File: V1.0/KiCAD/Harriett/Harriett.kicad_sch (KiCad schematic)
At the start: 21 parts, among them J1 Conn_02x08_Odd_Even, Q1 TP0604, Q2 2N3904, U1 ButtonPad_2x2, U2 DFRobotMP3PlayerMini, U4 BlackPill_F401CC

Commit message: Catchup
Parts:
- removed C1: 470u 16V, symbol Device:C_Polarized_Small
- removed J1: Conn_02x08_Odd_Even, symbol Connector_Generic:Conn_02x08_Odd_Even
- removed U1: ButtonPad_2x2, symbol UKMaker:ButtonPad_2x2
- added BT4: AA, symbol Device:Battery_Cell
- added D1: D, symbol Device:D
- added Q3: NPN, symbol Simulation_SPICE:NPN
- added Q4: Q_PMOS_DGS, symbol Device:Q_PMOS_DGS
- added R3: 22R, symbol Device:R
- added R4: R, symbol Device:R
- added R8: 100K, symbol Device:R
- added S1, S2, S3, S4: ~, SparkFun-KSA_SEALED_TAC_SWITCH, symbol Sparkfun:TAC_SWITCHKSA_SEALED
- Q1: symbol Device:Q_PMOS_DGS -> Device:Q_PMOS_SGD
- R5: value 1K -> 47k
- R6: value 1K -> 100K
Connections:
- net B10 is gone; now on net DF3_EN: U4.21 (B10)
- net +5V: now also Q1.1 (S), D1.1 (K); no longer BT3.1 (+), Q1.3 (S), R1.1
- net DF3_EN: no longer U4.19 (B1)
- net GND: now also R5.2, Q3.3 (E), R8.1, S1.2, S2.2, S3.2, S4.2
- net HARRIETT: now also U4.43 (B7), S2.4; no longer U4.39 (B3)
- net SNOOZE: now also U4.46 (B9), S4.4; no longer U4.41 (B5)
- net STOP: now also U4.45 (B8), S3.4; no longer U4.40 (B4)
- net WORK: now also U4.42 (B6), S1.4; no longer U4.20 (B2)
- net at C2.1, U2.1 (VCC): now also Q1.3 (D); no longer Q1.1 (D)
- net at U2.6 (SPK_1): now also R3.1; no longer LS1.2
- net at R5.1: now also R6.2, Q3.2 (B); no longer U4.25 (B12)
- net at U4.26 (B13): no longer R6.1
- net at U4.27 (B14): no longer R7.1
- net RST: now reaches R7.2
- net RST: now also R6.1
- net A11: no longer names the net of U4.32 (A11)
- net A12: no longer names the net of U4.33 (A12)
- net A15: no longer names the net of U4.38 (A15)
- net A6: no longer names the net of U4.16 (A6)
- net A8: no longer names the net of U4.29 (A8)
- net B15: no longer names the net of U4.28 (B15)
- net C13: no longer names the net of U4.2 (C13)
- net C14: no longer names the net of U4.3 (C14)
- net C15: no longer names the net of U4.4 (C15)
- net RX: no longer names the net of U4.31 (A10)
- net RX: no longer U2.3 (TX)
- net TX: no longer names the net of U4.30 (A9)
- net TX: no longer U2.2 (RX)
- new net: BT3.1 (+), BT4.2 (-)
- new net: Q3.1 (C), Q4.2 (G), R4.2
- new net: LS1.2, R3.2
- new net +6V: BT4.1 (+), D1.2 (A), R1.1
- new net DF3_RX: U2.3 (TX), U4.19 (B1)
- new net DF3_TX: U2.2 (RX), U4.20 (B2)
- new net EN: R7.1, R8.2
- new net VC: Q4.3 (S), R4.1
- new net VCC: Q4.1 (D)
- no-connect marks 13 -> 14
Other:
- note added: "0.6uA in shutdown mode for the power amp IC"
- note added: "5V -> 3.3V regulator on-board BlackPill is XC6219 (Marked LB2K) 25uA power consumption Specified for 2.0V to 6.0V input, absolute max 7.0V Dropout voltage 200mV So ideal for use with e.g. 3 or 4 x AA batteries"
- note added: "IRST = 3V3 / 101K + (3V3 - 0V7) / 100K = 33uA + 26uA = 59uA"
- note added: "Power consumption update max 40mW => 12mA Standby 0.017mW => 5.2uA"
- note removed: "1.5mA LED current Pins can do 8mA or 20mA with level loss"
- note removed: "5V -> 3.3V regulator on-board BlackPill is XC6219 (Marked LB2K) 25uA power consumption Specified for 2.0V to 6.0V input, absolute max 7.0V Dropout voltage 200mV So ideal for use with e.g. 3 x AA batteries"
- note removed: "Board outlines for diodes are populated with shorts"
- moved on the sheet: R1, R2

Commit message: Various updates backported from EDAWin - may be broken
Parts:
- added J1: Conn_01x04, symbol Connector_Generic:Conn_01x04
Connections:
- net +3.3V: now also J1.3 (Pin_3)
- net DF3_RX: now also U4.13 (A3); no longer U4.19 (B1)
- net DF3_TX: now also U4.12 (A2); no longer U4.20 (B2)
- net GND: now also J1.4 (Pin_4)
- net at U3.2 (RST): now also U4.19 (B1); no longer U4.12 (A2)
- net at U3.3 (DC): now also U4.20 (B2); no longer U4.13 (A3)
- net TX: now reaches U4.30 (A9)
- net TX: now also J1.2 (Pin_2)
- net RX: now reaches U4.31 (A10)
- net RX: now also J1.1 (Pin_1)
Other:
- note added: "Serial debugging"

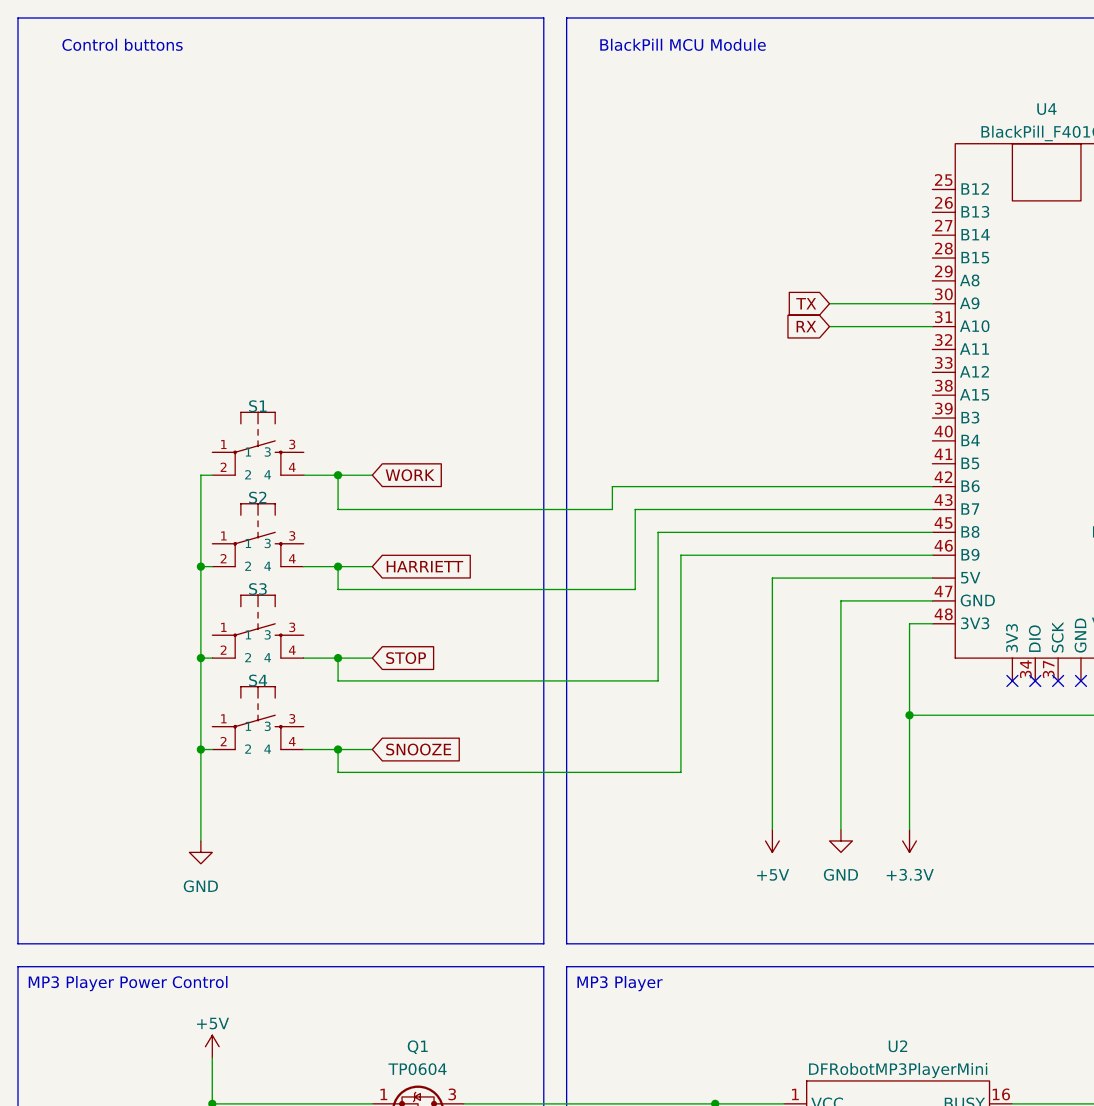
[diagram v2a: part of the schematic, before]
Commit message: Removed old Cura files. Updated schematic for PWM option
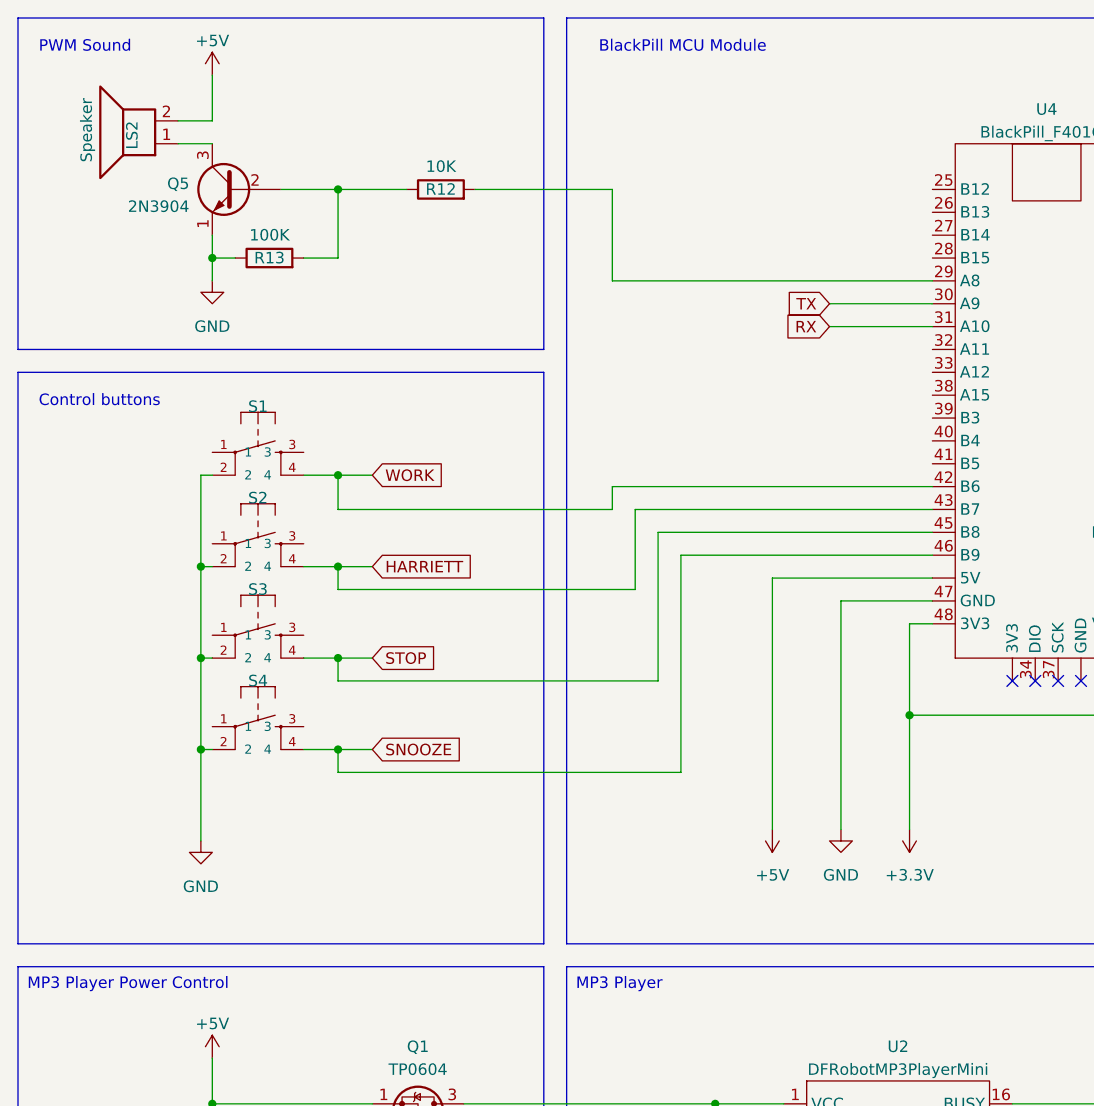
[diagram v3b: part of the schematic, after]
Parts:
- added LS2: Speaker, symbol Device:Speaker
- added Q5: 2N3904, symbol Device:Q_NPN_EBC
- added R12: 10K, symbol Device:R
- added R13: 100K, symbol Device:R
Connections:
- net +5V: now also LS2.2
- net GND: now also Q5.1 (E), R13.1
- net at U4.29 (A8): now also R12.2
- new net: Q5.2 (B), R12.1, R13.2
- new net: LS2.1, Q5.3 (C)
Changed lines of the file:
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@@
   (junction (at 327.66 93.98) (diameter 0) (color 0 0 0 0)
   )
+  (junction (at 57.15 46.99) (diameter 0) (color 0 0 0 0)
+  )
   (junction (at 327.66 76.2) (diameter 0) (color 0 0 0 0)
   )
@@
   )
   (junction (at 80.01 170.18) (diameter 0) (color 0 0 0 0)
+  )
+  (junction (at 71.12 39.37) (diameter 0) (color 0 0 0 0)
   )
   (junction (at 71.12 101.6) (diameter 0) (color 0 0 0 0)
@@
     (stroke (width 0) (type default))
   )
+  (wire (pts (xy 71.12 46.99) (xy 71.12 39.37))
+    (stroke (width 0) (type default))
+  )
   (wire (pts (xy 184.15 92.71) (xy 184.15 100.33))
     (stroke (width 0) (type default))
@@
     (stroke (width 0) (type default))
   )
+  (wire (pts (xy 86.36 39.37) (xy 101.6 39.37))
+    (stroke (width 0) (type default))
+  )
   (wire (pts (xy 219.71 96.52) (xy 210.82 96.52))
     (stroke (width 0) (type default))
@@
     (stroke (width 0) (type default))
   )
+  (wire (pts (xy 57.15 31.75) (xy 57.15 26.67))
+    (stroke (width 0) (type default))
+  )
   (wire (pts (xy 162.56 54.61) (xy 170.18 54.61))
     (stroke (width 0) (type default))
@@
     (stroke (width 0) (type default))
   )
+  (wire (pts (xy 57.15 46.99) (xy 57.15 49.53))
+    (stroke (width 0) (type default))
+  )
   (wire (pts (xy 127 85.09) (xy 127 110.49))
     (stroke (width 0) (type default))
@@
     (stroke (width 0) (type default))
   )
+  (wire (pts (xy 78.74 39.37) (xy 71.12 39.37))
+    (stroke (width 0) (type default))
+  )
   (wire (pts (xy 146.05 140.97) (xy 160.02 140.97))
     (stroke (width 0) (type default))
@@
     (stroke (width 0) (type default))
   )
+  (wire (pts (xy 53.34 31.75) (xy 57.15 31.75))
+    (stroke (width 0) (type default))
+  )
   (wire (pts (xy 101.6 72.39) (xy 101.6 74.93))
     (stroke (width 0) (type default))
@@
     (stroke (width 0) (type default))
   )
+  (wire (pts (xy 71.12 39.37) (xy 64.77 39.37))
+    (stroke (width 0) (type default))
+  )
   (wire (pts (xy 187.96 54.61) (xy 214.63 54.61))
     (stroke (width 0) (type default))
@@
     (stroke (width 0) (type default))
   )
+  (wire (pts (xy 53.34 34.29) (xy 57.15 34.29))
+    (stroke (width 0) (type default))
+  )
   (wire (pts (xy 113.03 140.97) (xy 120.65 140.97))
     (stroke (width 0) (type default))
@@
     (stroke (width 0) (type default))
   )
+  (wire (pts (xy 67.31 46.99) (xy 71.12 46.99))
+    (stroke (width 0) (type default))
+  )
   (wire (pts (xy 74.93 81.28) (xy 71.12 81.28))
     (stroke (width 0) (type default))
@@
     (stroke (width 0) (type default))
   )
+  (wire (pts (xy 57.15 44.45) (xy 57.15 46.99))
+    (stroke (width 0) (type default))
+  )
   (wire (pts (xy 109.22 146.05) (xy 120.65 146.05))
     (stroke (width 0) (type default))
@@
     (stroke (width 0) (type default))
   )
+  (wire (pts (xy 59.69 46.99) (xy 57.15 46.99))
+    (stroke (width 0) (type default))
+  )
   (wire (pts (xy 222.25 148.59) (xy 222.25 152.4))
     (stroke (width 0) (type default))
@@
     (stroke (width 0) (type default))
   )
+  (wire (pts (xy 101.6 49.53) (xy 101.6 39.37))
+    (stroke (width 0) (type default))
+  )
   (wire (pts (xy 85.09 140.97) (xy 113.03 140.97))
     (stroke (width 0) (type default))
@@
     (stroke (width 0) (type default))
   )
+  (wire (pts (xy 137.16 49.53) (xy 101.6 49.53))
+    (stroke (width 0) (type default))
+  )
   (wire (pts (xy 318.77 50.8) (xy 351.79 50.8))
     (stroke (width 0) (type default))
@@
     (fill (type none))
   )
+  (rectangle (start 35.56 20.32) (end 93.98 57.15)
+    (stroke (width 0) (type default))
+    (fill (type none))
+  )
   (rectangle (start 96.52 125.73) (end 175.26 191.77)
     (stroke (width 0) (type default))
@@
     (fill (type none))
   )
-  (rectangle (start 35.56 20.32) (end 93.98 123.19)
+  (rectangle (start 35.56 59.69) (end 93.98 123.19)
     (stroke (width 0) (type default))
     (fill (type none))
@@
   )
   (text_box "Control buttons"
-    (at 39.37 21.59 0) (size 24.13 3.81)
+    (at 36.83 60.96 0) (size 24.13 3.81)
     (stroke (width -0.0001) (type default))
     (fill (type color) (color 0 0 0 0))
@@
     (effects (font (size 1.27 1.27)) (justify left top))
   )
+  (text_box "PWM Sound"
+    (at 36.83 21.59 0) (size 24.13 3.81)
+    (stroke (width -0.0001) (type default))
+    (fill (type color) (color 0 0 0 0))
+    (effects (font (size 1.27 1.27)) (justify left top))
+  )
   (text_box "Battery power"
     (at 180.34 125.73 0) (size 16.51 3.81)
@@
         (path "/09e7eba4-d4fa-44e7-a6c2-fe424672ab5f"
           (reference "#PWR016") (unit 1)
+        )
+      )
+    )
+  )
+  (symbol (lib_id "Device:R") (at 82.55 39.37 90) (unit 1)
+    (in_bom yes) (on_board yes) (dnp no)
+    (property "Reference" "R12" (at 82.55 39.37 90)
+      (effects (font (size 1.27 1.27)))
+    )
+    (property "Value" "10K" (at 82.55 36.83 90)
+      (effects (font (size 1.27 1.27)))
+    )
+    (property "Footprint" "" (at 82.55 41.148 90)
+      (effects (font (size 1.27 1.27)) hide)
+    )
+    (property "Datasheet" "~" (at 82.55 39.37 0)
+      (effects (font (size 1.27 1.27)) hide)
+    )
+    (pin "1")
+    (pin "2")
+    (instances
+      (project "Harriett"
+        (path "/09e7eba4-d4fa-44e7-a6c2-fe424672ab5f"
+          (reference "R12") (unit 1)
         )
       )
@@
     )
   )
+  (symbol (lib_id "Device:Speaker") (at 48.26 34.29 180) (unit 1)
+    (in_bom yes) (on_board yes) (dnp no)
+    (property "Reference" "LS2" (at 48.26 31.75 90)
+      (effects (font (size 1.27 1.27)) (justify left))
+    )
+    (property "Value" "Speaker" (at 43.18 29.21 90)
+      (effects (font (size 1.27 1.27)) (justify left))
+    )
+    (property "Footprint" "" (at 48.26 29.21 0)
+      (effects (font (size 1.27 1.27)) hide)
+    )
+    (property "Datasheet" "~" (at 48.514 33.02 0)
+      (effects (font (size 1.27 1.27)) hide)
+    )
+    (pin "1")
+    (pin "2")
+    (instances
+      (project "Harriett"
+        (path "/09e7eba4-d4fa-44e7-a6c2-fe424672ab5f"
+          (reference "LS2") (unit 1)
+        )
+      )
+    )
+  )
   (symbol (lib_id "Device:Battery_Cell") (at 222.25 146.05 0) (unit 1)
     (in_bom yes) (on_board yes) (dnp no)
@@
     )
   )
+  (symbol (lib_id "power:+5V") (at 57.15 26.67 0) (unit 1)
+    (in_bom yes) (on_board yes) (dnp no) (fields_autoplaced)
+    (property "Reference" "#PWR018" (at 57.15 30.48 0)
+      (effects (font (size 1.27 1.27)) hide)
+    )
+    (property "Value" "+5V" (at 57.15 22.86 0)
+      (effects (font (size 1.27 1.27)))
+    )
+    (property "Footprint" "" (at 57.15 26.67 0)
+      (effects (font (size 1.27 1.27)) hide)
+    )
+    (property "Datasheet" "" (at 57.15 26.67 0)
+      (effects (font (size 1.27 1.27)) hide)
+    )
+    (pin "1")
+    (instances
+      (project "Harriett"
+        (path "/09e7eba4-d4fa-44e7-a6c2-fe424672ab5f"
+          (reference "#PWR018") (unit 1)
+        )
+      )
+    )
+  )
+  (symbol (lib_id "power:GND") (at 57.15 49.53 0) (unit 1)
+    (in_bom yes) (on_board yes) (dnp no) (fields_autoplaced)
+    (property "Reference" "#PWR015" (at 57.15 55.88 0)
+      (effects (font (size 1.27 1.27)) hide)
+    )
+    (property "Value" "GND" (at 57.15 54.61 0)
+      (effects (font (size 1.27 1.27)))
+    )
+    (property "Footprint" "" (at 57.15 49.53 0)
+      (effects (font (size 1.27 1.27)) hide)
+    )
+    (property "Datasheet" "" (at 57.15 49.53 0)
+      (effects (font (size 1.27 1.27)) hide)
+    )
+    (pin "1")
+    (instances
+      (project "Harriett"
+        (path "/09e7eba4-d4fa-44e7-a6c2-fe424672ab5f"
+          (reference "#PWR015") (unit 1)
+        )
+      )
+    )
+  )
+  (symbol (lib_id "Device:Q_NPN_EBC") (at 59.69 39.37 0) (mirror y) (unit 1)
+    (in_bom yes) (on_board yes) (dnp no) (fields_autoplaced)
+    (property "Reference" "Q5" (at 54.61 38.735 0)
+      (effects (font (size 1.27 1.27)) (justify left))
+    )
+    (property "Value" "2N3904" (at 54.61 41.275 0)
+      (effects (font (size 1.27 1.27)) (justify left))
+    )
+    (property "Footprint" "" (at 54.61 36.83 0)
+      (effects (font (size 1.27 1.27)) hide)
+    )
+    (property "Datasheet" "~" (at 59.69 39.37 0)
+      (effects (font (size 1.27 1.27)) hide)
+    )
+    (pin "1")
+    (pin "2")
+    (pin "3")
+    (instances
+      (project "Harriett"
+        (path "/09e7eba4-d4fa-44e7-a6c2-fe424672ab5f"
+          (reference "Q5") (unit 1)
+        )
+      )
+    )
+  )
   (symbol (lib_id "Device:Q_NPN_EBC") (at 77.47 162.56 0) (unit 1)
     (in_bom yes) (on_board yes) (dnp no) (fields_autoplaced)
@@
         )
       )
+    )
+  )
+  (symbol (lib_id "Device:R") (at 63.5 46.99 90) (unit 1)
+    (in_bom yes) (on_board yes) (dnp no)
+    (property "Reference" "R13" (at 63.5 46.99 90)
+      (effects (font (size 1.27 1.27)))
+    )
+    (property "Value" "100K" (at 63.5 44.45 90)
+      (effects (font (size 1.27 1.27)))
+    )
+    (property "Footprint" "" (at 63.5 48.768 90)
+      (effects (font (size 1.27 1.27)) hide)
+    )
+    (property "Datasheet" "~" (at 63.5 46.99 0)
+      (effects (font (size 1.27 1.27)) hide)
+    )
+    (pin "1")
+    (pin "2")
+    (instances
+      (project "Harriett"
+        (path "/09e7eba4-d4fa-44e7-a6c2-fe424672ab5f"
+          (reference "R13") (unit 1)
+        )
+      )
